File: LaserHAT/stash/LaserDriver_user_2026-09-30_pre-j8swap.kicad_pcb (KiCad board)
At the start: 2 copper layers, 65 x 56.9 mm, 58 parts, among them J1 GPIO, J5 USB_C_Receptacle_USB2.0_16P, J6 BNC TRIGGER IN, J7 BNC STIM OUT, J8 DB_POWER_TIMING, J9 DB_ANALOG, Q3 AP30P30Q, Q4 DMMT5401, Q5 AP30P30Q, SW10 USB PWR, SW6 BSL, SW7 BL-DT (LCSC C53223909), SW8 BACK, SW9 FIRE, U1 CAT24C32, U4 MCP1700x-330xxMB, U5 AP2171W, U6 CH340N, U7 MSPM0G3507SRHBR, U8 74LVC2G17

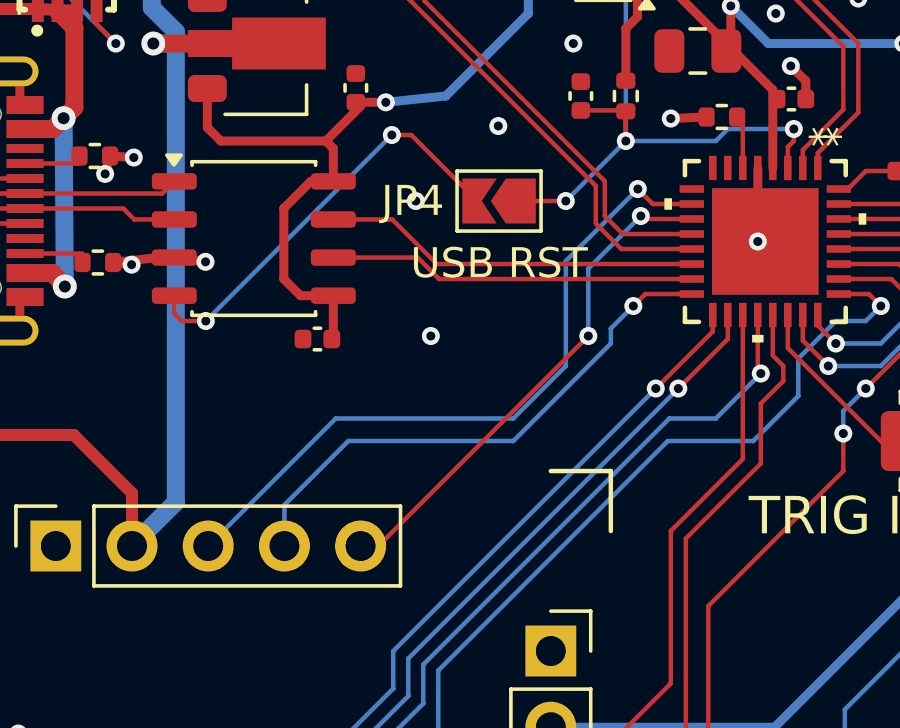
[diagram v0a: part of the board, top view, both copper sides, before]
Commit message: LaserHAT: J8.3 = FAULT_n (PA6), J8.5 = EN/PWM_A (PA7) on the HAT and the laser module
Follows the e-stim module's connector standard (spec §3/§7, LAYOUT_HANDOFF Q2):
- bnc_daughter_io.kicad_sch: DB_GPIO on J8.3, DB_PWM_A on J8.5 (rev2_migrate.py matches)
- LaserDriver.kicad_pcb: J8 pads re-netted, PA6/PA7 traces re-routed along the old
  corridors (same vias at U7); DRC unchanged, 0 unconnected; backup in stash/
- LaserDaughter: J1.5 = DB_PWM_A, J1.3 n/c; schematic regenerated, board re-routed
- REV2_NOTES/CLAUDE.md: PA17/PA22 rows now say I2C SDA/SCL; note on why hardware I2C1
  cannot use them and the re-map that would (J9.4 -> PA16, J9.5 -> PA17, BUTTON3 -> PA22)
- LAYOUT_HANDOFF Q1/Q2 answered, spec §7 marked applied, fab outputs regenerated
- tools/schlib.py: symbol dir from env / Linux default

Co-Authored-By: Claude Fable 5.1 <noreply@anthropic.com>
Claude-Session: https://claude.ai/code/session_018vgLizGzYPynnY93ajvoVA
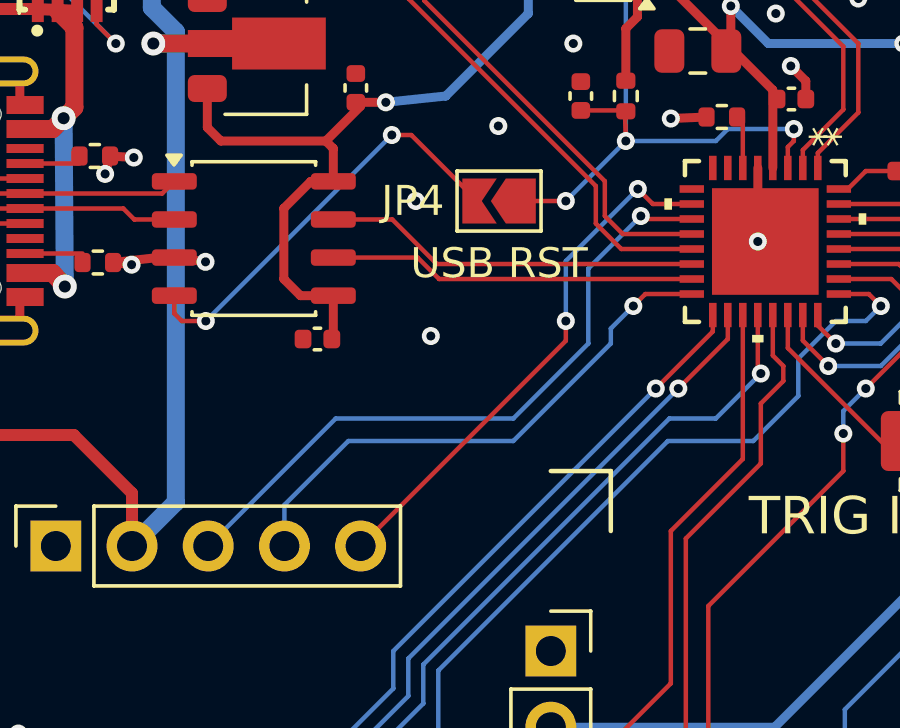
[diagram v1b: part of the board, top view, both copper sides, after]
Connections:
- J8 pad 3: DB_GPIO -> DB_PWM_A
- J8 pad 5: DB_PWM_A -> DB_GPIO
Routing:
- net DB_GPIO: track 23.3 -> 17.7 mm, vias 1 -> 2
- net DB_PWM_A: track 17.0 -> 22.2 mm, vias 2 -> 1
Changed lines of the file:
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@@
 			(layers "*.Cu" "*.Mask")
 			(remove_unused_layers no)
-			(net 66 "DB_GPIO")
+			(net 67 "DB_PWM_A")
 			(pinfunction "Pin_3")
 			(pintype "passive")
@@
 			(layers "*.Cu" "*.Mask")
 			(remove_unused_layers no)
-			(net 67 "DB_PWM_A")
+			(net 66 "DB_GPIO")
 			(pinfunction "Pin_5")
 			(pintype "passive")
@@
 	)
 	(segment
-		(start 128.9 67.099999)
-		(end 128.4 66.599999)
+		(start 128.90063 67.09937)
+		(end 128.40063 66.599369)
 		(width 0.15)
-		(locked yes)
 		(layer "F.Cu")
 		(net 66)
 	)
 	(segment
-		(start 130.198711 67.099369)
-		(end 128.9 67.099999)
+		(start 126 71.66)
+		(end 126 71)
 		(width 0.15)
-		(locked yes)
 		(layer "F.Cu")
 		(net 66)
 	)
-	(via
-		(at 128.4 66.599999)
-		(size 0.6)
-		(drill 0.3)
-		(layers "F.Cu" "B.Cu")
-		(locked yes)
-		(net 66)
-	)
 	(segment
-		(start 118.33 74.25)
-		(end 114.08 78.5)
+		(start 128.90063 67.09937)
+		(end 130.198711 67.09937)
 		(width 0.15)
-		(locked yes)
-		(layer "B.Cu")
+		(layer "F.Cu")
 		(net 66)
 	)
 	(segment
-		(start 126 72.5)
-		(end 124.25 74.25)
+		(start 119.16 78.5)
+		(end 126 71.66)
 		(width 0.15)
-		(locked yes)
-		(layer "B.Cu")
+		(layer "F.Cu")
 		(net 66)
 	)
-	(segment
-		(start 128.4 66.599999)
-		(end 126 69)
-		(width 0.15)
-		(locked yes)
-		(layer "B.Cu")
+	(via
+		(at 128.40063 66.599369)
+		(size 0.6)
+		(drill 0.3)
+		(layers "F.Cu" "B.Cu")
+		(net 66)
+	)
+	(via
+		(at 126 71)
+		(size 0.6)
+		(drill 0.3)
+		(layers "F.Cu" "B.Cu")
 		(net 66)
 	)
 	(segment
-		(start 124.25 74.25)
-		(end 118.33 74.25)
+		(start 126 71)
+		(end 126 69)
 		(width 0.15)
-		(locked yes)
 		(layer "B.Cu")
 		(net 66)
@@
 	(segment
 		(start 126 69)
-		(end 126 72.5)
+		(end 128.40063 66.599369)
 		(width 0.15)
-		(locked yes)
 		(layer "B.Cu")
 		(net 66)
 	)
 	(segment
-		(start 119.75 78.5)
-		(end 119.16 78.5)
+		(start 128.599496 67.599496)
+		(end 128.5 67.5)
 		(width 0.15)
-		(locked yes)
 		(layer "F.Cu")
 		(net 67)
@@
 	(segment
 		(start 130.198711 67.599496)
-		(end 128.6 67.6)
+		(end 128.599496 67.599496)
 		(width 0.15)
-		(locked yes)
 		(layer "F.Cu")
 		(net 67)
 	)
-	(segment
-		(start 126.75 71.5)
-		(end 119.75 78.5)
-		(width 0.15)
-		(locked yes)
-		(layer "F.Cu")
+	(via
+		(at 128.5 67.5)
+		(size 0.6)
+		(drill 0.3)
+		(layers "F.Cu" "B.Cu")
 		(net 67)
 	)
 	(segment
-		(start 128.6 67.6)
-		(end 128.5 67.5)
+		(start 118.33 74.25)
+		(end 124.25 74.25)
 		(width 0.15)
-		(locked yes)
-		(layer "F.Cu")
+		(layer "B.Cu")
 		(net 67)
 	)
-	(via
-		(at 126.75 71.5)
-		(size 0.6)
-		(drill 0.3)
-		(layers "F.Cu" "B.Cu")
-		(locked yes)
+	(segment
+		(start 126.75 71.75)
+		(end 126.75 69.25)
+		(width 0.15)
+		(layer "B.Cu")
 		(net 67)
 	)
-	(via
-		(at 128.5 67.5)
-		(size 0.6)
-		(drill 0.3)
-		(layers "F.Cu" "B.Cu")
-		(locked yes)
+	(segment
+		(start 124.25 74.25)
+		(end 126.75 71.75)
+		(width 0.15)
+		(layer "B.Cu")
 		(net 67)
 	)
@@
 		(end 126.75 69.25)
 		(width 0.15)
-		(locked yes)
 		(layer "B.Cu")
 		(net 67)
 	)
 	(segment
-		(start 126.75 69.25)
-		(end 126.75 71.5)
+		(start 114.08 78.5)
+		(end 118.33 74.25)
 		(width 0.15)
-		(locked yes)
 		(layer "B.Cu")
 		(net 67)
